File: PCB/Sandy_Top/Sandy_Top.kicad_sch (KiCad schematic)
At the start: 74 parts, among them J1 Conn_02x02_Top_Bottom, J2 Conn_02x02_Top_Bottom, J3 Conn_02x02_Top_Bottom

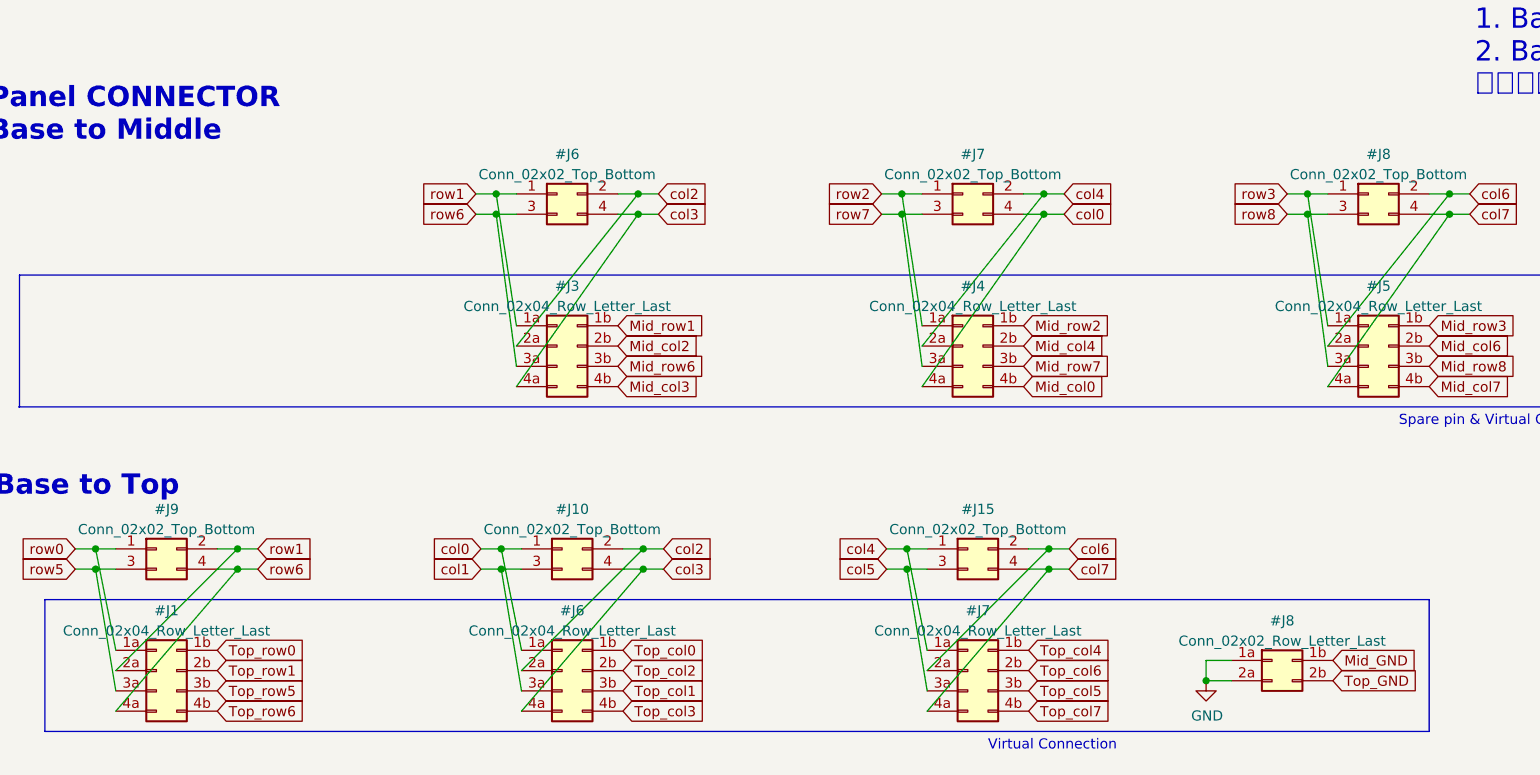
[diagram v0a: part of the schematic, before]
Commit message: ネジ穴のフットプリントをわかりやすく
これまでKiCadのライブラリに保存していたフットプリントを、ローカルへ移動。
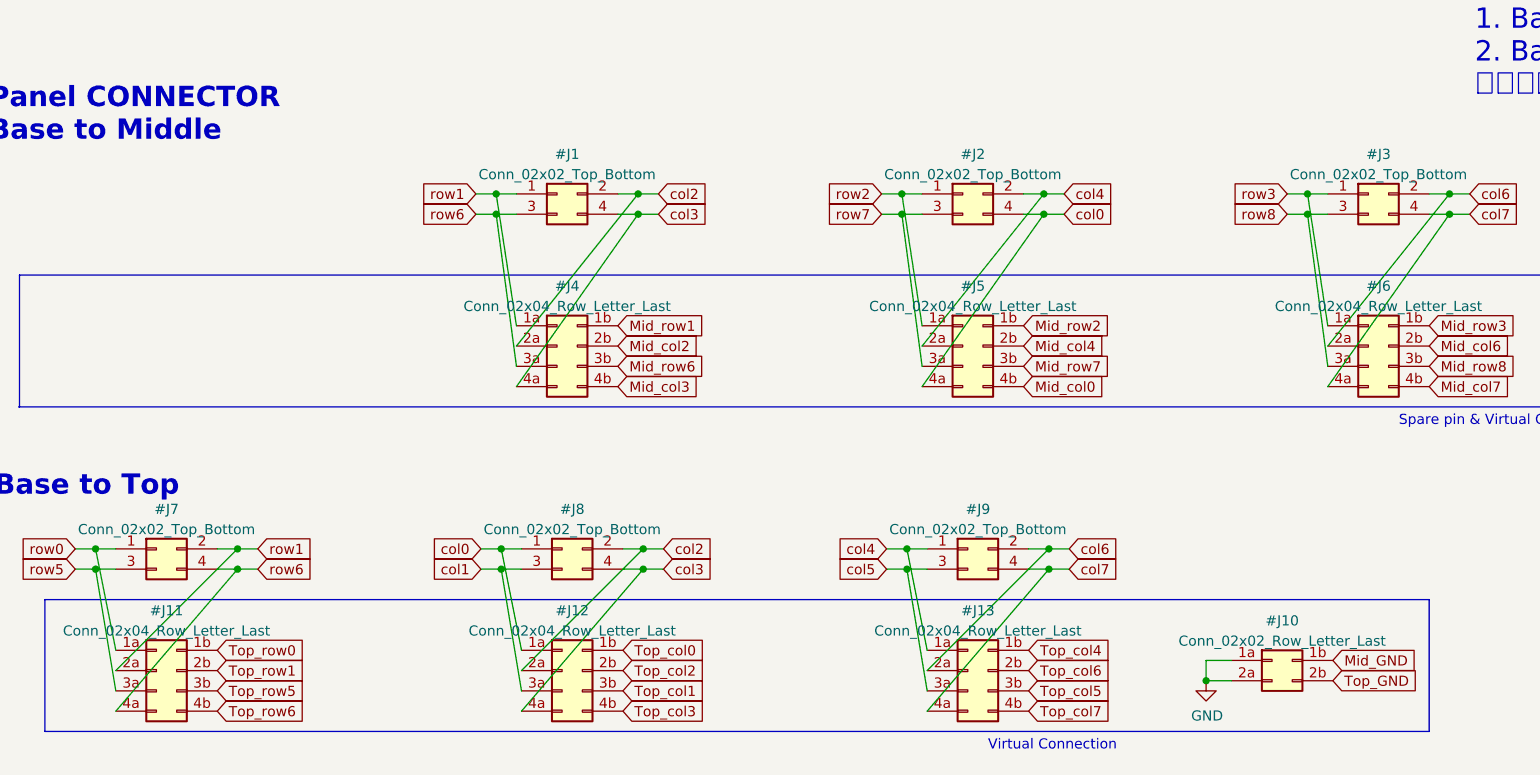
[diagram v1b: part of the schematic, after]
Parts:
- H1, H2, H3, H4, H5, H6, H7, H8: footprint MountingHole:MountingHole_2.2mm_M2_Pad_minimal -> locallib:MountingHole_2.2mm_M2_Pad_minimal
- renumbered #J6 to #J1, #J8 to #J10, #J1 to #J11, #J6 to #J12, #J7 to #J13, #J7 to #J2, #J8 to #J3, #J3 to #J4, #J4 to #J5, #J5 to #J6, #J9 to #J7, #J10 to #J8, #J15 to #J9

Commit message: ダイオードの方向を強調するシルクに変更
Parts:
- D1, D10, D11, D12, D13, D14, D15, D16, D17, D18, D19, D2, D3, D4, D5, D6, D7, D8, D9: footprint Diode_SMD:D_SOD-123 -> locallib:D_SOD-123_Emphasized_Direction_Line

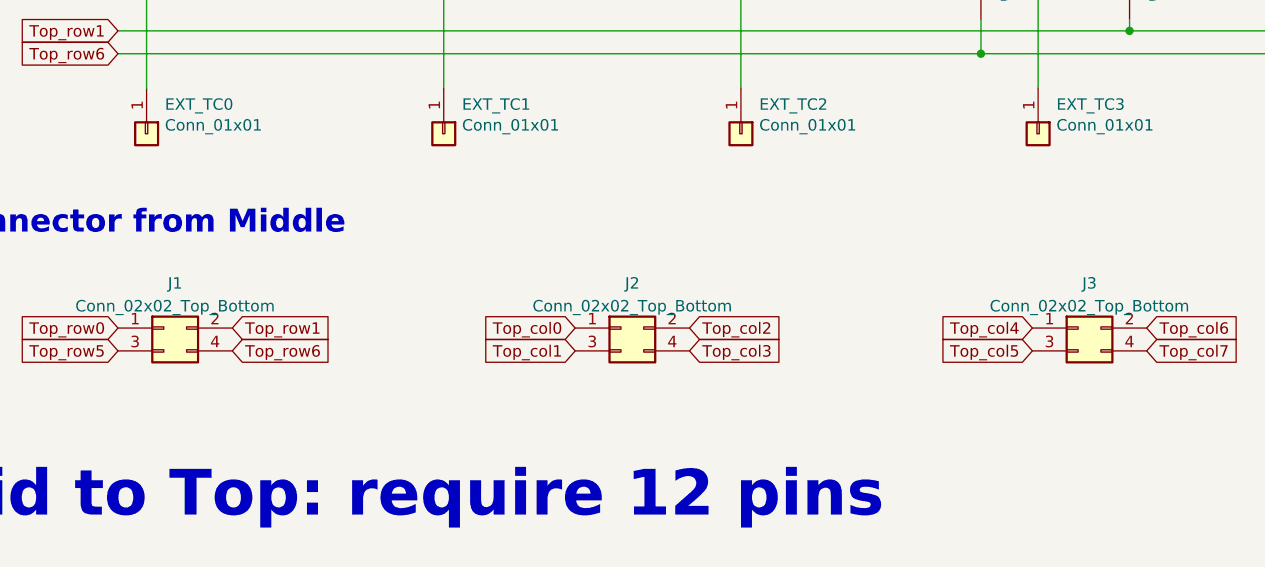
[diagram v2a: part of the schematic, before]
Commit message: "Back Side"シルク位置調整
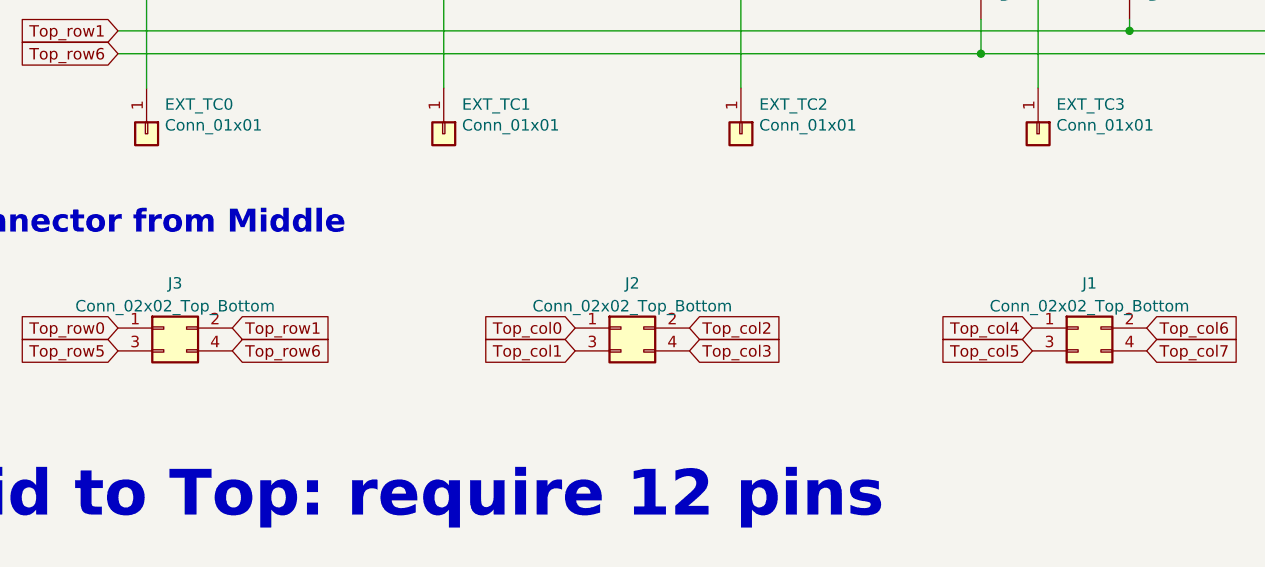
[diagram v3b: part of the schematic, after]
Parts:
- renumbered J3 to J1, J1 to J3
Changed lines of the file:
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@@
   (symbol (lib_id "Connector_Generic:Conn_02x02_Odd_Even") (at 41.275 122.555 0) (unit 1)
     (in_bom yes) (on_board yes) (fields_autoplaced)
-    (property "Reference" "J1" (id 0) (at 42.545 117.5852 0))
+    (property "Reference" "J3" (id 0) (at 42.545 117.5852 0))
     (property "Value" "Conn_02x02_Top_Bottom" (id 1) (at 42.545 120.1221 0))
     (property "Footprint" "locallib:JST_SH_SM04B-SRSS-TB_1x04-1MP_P1.00mm_Horizontal_wCable_housing_spare_pin" (id 2) (at 41.275 122.555 0)
@@
   (symbol (lib_id "Connector_Generic:Conn_02x02_Odd_Even") (at 142.875 122.555 0) (unit 1)
     (in_bom yes) (on_board yes) (fields_autoplaced)
-    (property "Reference" "J3" (id 0) (at 144.145 117.5852 0))
+    (property "Reference" "J1" (id 0) (at 144.145 117.5852 0))
     (property "Value" "Conn_02x02_Top_Bottom" (id 1) (at 144.145 120.1221 0))
     (property "Footprint" "locallib:JST_SH_SM04B-SRSS-TB_1x04-1MP_P1.00mm_Horizontal_wCable_housing_spare_pin" (id 2) (at 142.875 122.555 0)
@@
       (reference "H8") (unit 1) (value "MountingHole") (footprint "locallib:MountingHole_2.2mm_M2_Pad_minimal")
     )
-    (path "/90388007-91e1-4316-b56b-700ec855e189"
+    (path "/a59ce6ab-5ea8-40d7-a5d1-8b6575f83fa0"
       (reference "J1") (unit 1) (value "Conn_02x02_Top_Bottom") (footprint "locallib:JST_SH_SM04B-SRSS-TB_1x04-1MP_P1.00mm_Horizontal_wCable_housing_spare_pin")
     )
@@
       (reference "J2") (unit 1) (value "Conn_02x02_Top_Bottom") (footprint "locallib:JST_SH_SM04B-SRSS-TB_1x04-1MP_P1.00mm_Horizontal_wCable_housing_spare_pin")
     )
-    (path "/a59ce6ab-5ea8-40d7-a5d1-8b6575f83fa0"
+    (path "/90388007-91e1-4316-b56b-700ec855e189"
       (reference "J3") (unit 1) (value "Conn_02x02_Top_Bottom") (footprint "locallib:JST_SH_SM04B-SRSS-TB_1x04-1MP_P1.00mm_Horizontal_wCable_housing_spare_pin")
     )

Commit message: SHコネクタのパーツ番号を追加
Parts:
- J1, J2, J3: LCSC (none) -> C371510
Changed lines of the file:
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@@
+      (effects (font (size 1.27 1.27)) hide)
+    )
+    (property "LCSC" "C371510" (id 4) (at 92.075 122.555 0)
       (effects (font (size 1.27 1.27)) hide)
     )
@@
       (effects (font (size 1.27 1.27)) hide)
     )
+    (property "LCSC" "C371510" (id 4) (at 41.275 122.555 0)
+      (effects (font (size 1.27 1.27)) hide)
+    )
     (pin "1")
     (pin "2")
@@
       (effects (font (size 1.27 1.27)) hide)
     )
+    (property "LCSC" "C371510" (id 4) (at 142.875 122.555 0)
+      (effects (font (size 1.27 1.27)) hide)
+    )

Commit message: WIP, issue #61
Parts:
- renumbered J3 to J2, J2 to J3

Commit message: Top v02（外形変更はまだ）
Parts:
- SW_-1, SW_1, SW_10, SW_2, SW_3, SW_4, SW_7, SW_9, SW_=1, SW_ESC1, SW_T1, SW_Y1, SW_[1, SW_\1, SW_]1, SW_`1: footprint MX_Alps_Hybrid:MXOnly-1U-NoLED -> MX_Alps_Hybrid:MXOnly-1U-Hotswap-guide
- SW_5: footprint MX_Alps_Hybrid:MXOnly-1U-NoLED -> MX_Alps_Hybrid:MXOnly-1U-Hotswap-screw-hole-side2-guide
- SW_6: footprint MX_Alps_Hybrid:MXOnly-1U-NoLED -> MX_Alps_Hybrid:MXOnly-1U-Hotswap-screw-hole-side1-guide
- SW_8: footprint MX_Alps_Hybrid:MXOnly-1U-NoLED -> MX_Alps_Hybrid:MXOnly-1U-Hotswap-screw-hole-side3-guide
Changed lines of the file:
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@@
       (effects (font (size 1.27 1.27)))
     )
-    (property "Footprint" "MX_Alps_Hybrid:MXOnly-1U-NoLED" (at 44.45 43.815 0)
+    (property "Footprint" "MX_Alps_Hybrid:MXOnly-1U-Hotswap-guide" (at 44.45 43.815 0)
       (effects (font (size 1.27 1.27)) hide)
     )
@@
       (effects (font (size 1.27 1.27)))
     )
-    (property "Footprint" "MX_Alps_Hybrid:MXOnly-1U-NoLED" (at 193.04 43.815 0)
+    (property "Footprint" "MX_Alps_Hybrid:MXOnly-1U-Hotswap-guide" (at 193.04 43.815 0)
       (effects (font (size 1.27 1.27)) hide)
     )
@@
       (effects (font (size 1.27 1.27)))
     )
-    (property "Footprint" "MX_Alps_Hybrid:MXOnly-1U-NoLED" (at 77.47 43.815 0)
+    (property "Footprint" "MX_Alps_Hybrid:MXOnly-1U-Hotswap-guide" (at 77.47 43.815 0)
       (effects (font (size 1.27 1.27)) hide)
     )
@@
       (effects (font (size 1.27 1.27)))
     )
-    (property "Footprint" "MX_Alps_Hybrid:MXOnly-1U-NoLED" (at 143.51 43.815 0)
+    (property "Footprint" "MX_Alps_Hybrid:MXOnly-1U-Hotswap-screw-hole-side1-guide" (at 143.51 43.815 0)
       (effects (font (size 1.27 1.27)) hide)
     )
@@
       (effects (font (size 1.27 1.27)))
     )
-    (property "Footprint" "MX_Alps_Hybrid:MXOnly-1U-NoLED" (at 127 75.565 0)
+    (property "Footprint" "MX_Alps_Hybrid:MXOnly-1U-Hotswap-guide" (at 127 75.565 0)
       (effects (font (size 1.27 1.27)) hide)
     )
@@
       (effects (font (size 1.27 1.27)))
     )
-    (property "Footprint" "MX_Alps_Hybrid:MXOnly-1U-NoLED" (at 160.02 43.815 0)
+    (property "Footprint" "MX_Alps_Hybrid:MXOnly-1U-Hotswap-guide" (at 160.02 43.815 0)
       (effects (font (size 1.27 1.27)) hide)
     )
@@
       (effects (font (size 1.27 1.27)))
     )
-    (property "Footprint" "MX_Alps_Hybrid:MXOnly-1U-NoLED" (at 259.08 43.815 0)
+    (property "Footprint" "MX_Alps_Hybrid:MXOnly-1U-Hotswap-guide" (at 259.08 43.815 0)
       (effects (font (size 1.27 1.27)) hide)
     )
@@
       (effects (font (size 1.27 1.27)))
     )
-    (property "Footprint" "MX_Alps_Hybrid:MXOnly-1U-NoLED" (at 209.55 43.815 0)
+    (property "Footprint" "MX_Alps_Hybrid:MXOnly-1U-Hotswap-screw-hole-side3-guide" (at 209.55 43.815 0)
       (effects (font (size 1.27 1.27)) hide)
     )
@@
       (effects (font (size 1.27 1.27)))
     )
-    (property "Footprint" "MX_Alps_Hybrid:MXOnly-1U-NoLED" (at 60.96 43.815 0)
+    (property "Footprint" "MX_Alps_Hybrid:MXOnly-1U-Hotswap-guide" (at 60.96 43.815 0)
       (effects (font (size 1.27 1.27)) hide)
     )
@@
       (effects (font (size 1.27 1.27)))
     )
-    (property "Footprint" "MX_Alps_Hybrid:MXOnly-1U-NoLED" (at 127 43.815 0)
+    (property "Footprint" "MX_Alps_Hybrid:MXOnly-1U-Hotswap-screw-hole-side2-guide" (at 127 43.815 0)
       (effects (font (size 1.27 1.27)) hide)
     )
@@
       (effects (font (size 1.27 1.27)))
     )
-    (property "Footprint" "MX_Alps_Hybrid:MXOnly-1U-NoLED" (at 226.06 43.815 0)
+    (property "Footprint" "MX_Alps_Hybrid:MXOnly-1U-Hotswap-guide" (at 226.06 43.815 0)
       (effects (font (size 1.27 1.27)) hide)
     )
@@
       (effects (font (size 1.27 1.27)))
     )
-    (property "Footprint" "MX_Alps_Hybrid:MXOnly-1U-NoLED" (at 176.53 75.565 0)
+    (property "Footprint" "MX_Alps_Hybrid:MXOnly-1U-Hotswap-guide" (at 176.53 75.565 0)
       (effects (font (size 1.27 1.27)) hide)
     )
@@
       (effects (font (size 1.27 1.27)))
     )
-    (property "Footprint" "MX_Alps_Hybrid:MXOnly-1U-NoLED" (at 143.51 75.565 0)
+    (property "Footprint" "MX_Alps_Hybrid:MXOnly-1U-Hotswap-guide" (at 143.51 75.565 0)
       (effects (font (size 1.27 1.27)) hide)
     )
@@
       (effects (font (size 1.27 1.27)))
     )
-    (property "Footprint" "MX_Alps_Hybrid:MXOnly-1U-NoLED" (at 242.57 43.815 0)
+    (property "Footprint" "MX_Alps_Hybrid:MXOnly-1U-Hotswap-guide" (at 242.57 43.815 0)
       (effects (font (size 1.27 1.27)) hide)
     )
@@
       (effects (font (size 1.27 1.27)))
     )
-    (property "Footprint" "MX_Alps_Hybrid:MXOnly-1U-NoLED" (at 93.98 43.815 0)
+    (property "Footprint" "MX_Alps_Hybrid:MXOnly-1U-Hotswap-guide" (at 93.98 43.815 0)
       (effects (font (size 1.27 1.27)) hide)
     )
@@
       (effects (font (size 1.27 1.27)))
     )
-    (property "Footprint" "MX_Alps_Hybrid:MXOnly-1U-NoLED" (at 275.59 43.815 0)
+    (property "Footprint" "MX_Alps_Hybrid:MXOnly-1U-Hotswap-guide" (at 275.59 43.815 0)
       (effects (font (size 1.27 1.27)) hide)
     )
@@
       (effects (font (size 1.27 1.27)))
     )
-    (property "Footprint" "MX_Alps_Hybrid:MXOnly-1U-NoLED" (at 160.02 75.565 0)
+    (property "Footprint" "MX_Alps_Hybrid:MXOnly-1U-Hotswap-guide" (at 160.02 75.565 0)
       (effects (font (size 1.27 1.27)) hide)
     )
@@
       (effects (font (size 1.27 1.27)))
     )
-    (property "Footprint" "MX_Alps_Hybrid:MXOnly-1U-NoLED" (at 110.49 43.815 0)
+    (property "Footprint" "MX_Alps_Hybrid:MXOnly-1U-Hotswap-guide" (at 110.49 43.815 0)
       (effects (font (size 1.27 1.27)) hide)
     )
@@
       (effects (font (size 1.27 1.27)))
     )
-    (property "Footprint" "MX_Alps_Hybrid:MXOnly-1U-NoLED" (at 176.53 43.815 0)
-      (effects (font (size 1.27 1.27)) hide)
-    )
+    (property "Footprint" "MX_Alps_Hybrid:MXOnly-1U-Hotswap-guide" (at 176.53 43.815 0)
+      (effects (font (size 1.27 1.27)) hide)
+    )
